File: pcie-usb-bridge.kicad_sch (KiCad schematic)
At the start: 50 parts, among them IC1 UPD720201K8-711-BAC-A, U2 SST25VF512A, Y1 NX3225SA-24M

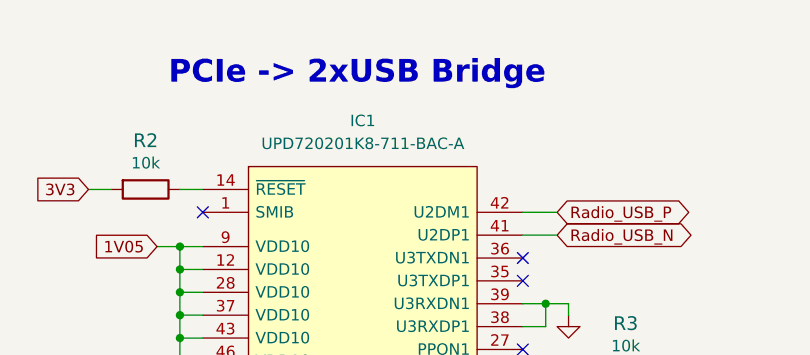
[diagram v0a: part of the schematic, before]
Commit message: Created FT2232 layout
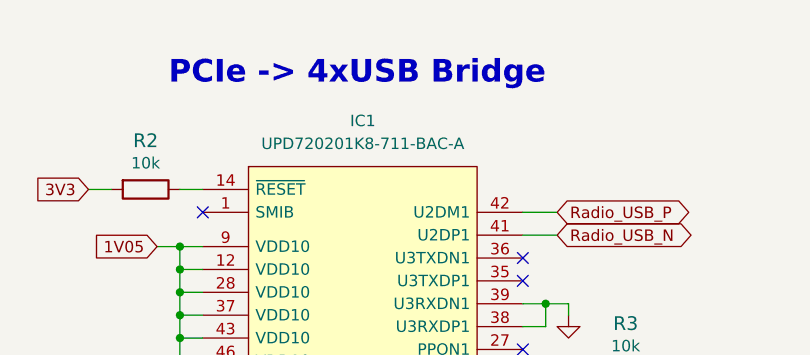
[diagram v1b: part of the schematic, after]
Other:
- note added: "PCIe -> 4xUSB Bridge"
- note removed: "PCIe -> 2xUSB Bridge"
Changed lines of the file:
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@@
   (title_block
     (title "M.2 Smart IoT Module")
-    (date "2021-08-11")
-    (rev "1.1.0")
+    (date "2022-07-11")
+    (rev "1.2.0")
     (comment 1 "www.antmicro.com")
     (comment 2 "Antmicro Ltd.")
@@
     (effects (font (size 1.27 1.27)) (justify left bottom))
   )
-  (text "PCIe -> 2xUSB Bridge" (at 71.12 20.32 0)
+  (text "PCIe -> 4xUSB Bridge" (at 71.12 20.32 0)
     (effects (font (size 2.5146 2.5146) (thickness 0.5029) bold) (justify left bottom))
   )

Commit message: Applied fixes to issues that came up in review
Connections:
- net Radio_USB_N: now also IC1.42 (U2DM1); no longer IC1.41 (U2DP1)
- net Radio_USB_P: now also IC1.41 (U2DP1); no longer IC1.42 (U2DM1)
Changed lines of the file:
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@@
     )
   )
-  (global_label "Radio_USB_P" (shape bidirectional) (at 114.3 34.29 0) (fields_autoplaced)
+  (global_label "Radio_USB_P" (shape bidirectional) (at 114.3 36.83 0) (fields_autoplaced)
     (effects (font (size 1.27 1.27)) (justify left))
-    (property "Intersheet References" "${INTERSHEET_REFS}" (id 0) (at 128.9613 34.2106 0)
+    (property "Intersheet References" "${INTERSHEET_REFS}" (id 0) (at 128.9613 36.7506 0)
       (effects (font (size 1.27 1.27)) (justify left) hide)
     )
@@
     )
   )
-  (global_label "Radio_USB_N" (shape bidirectional) (at 114.3 36.83 0) (fields_autoplaced)
+  (global_label "Radio_USB_N" (shape bidirectional) (at 114.3 34.29 0) (fields_autoplaced)
     (effects (font (size 1.27 1.27)) (justify left))
-    (property "Intersheet References" "${INTERSHEET_REFS}" (id 0) (at 129.0218 36.7506 0)
+    (property "Intersheet References" "${INTERSHEET_REFS}" (id 0) (at 129.0218 34.2106 0)
       (effects (font (size 1.27 1.27)) (justify left) hide)
     )
